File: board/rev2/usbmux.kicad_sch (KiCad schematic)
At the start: 5 parts, among them SW5 MS-22D28-G020, U18 TS3USB30ERSWR, U2 TS3USB30ERSWR

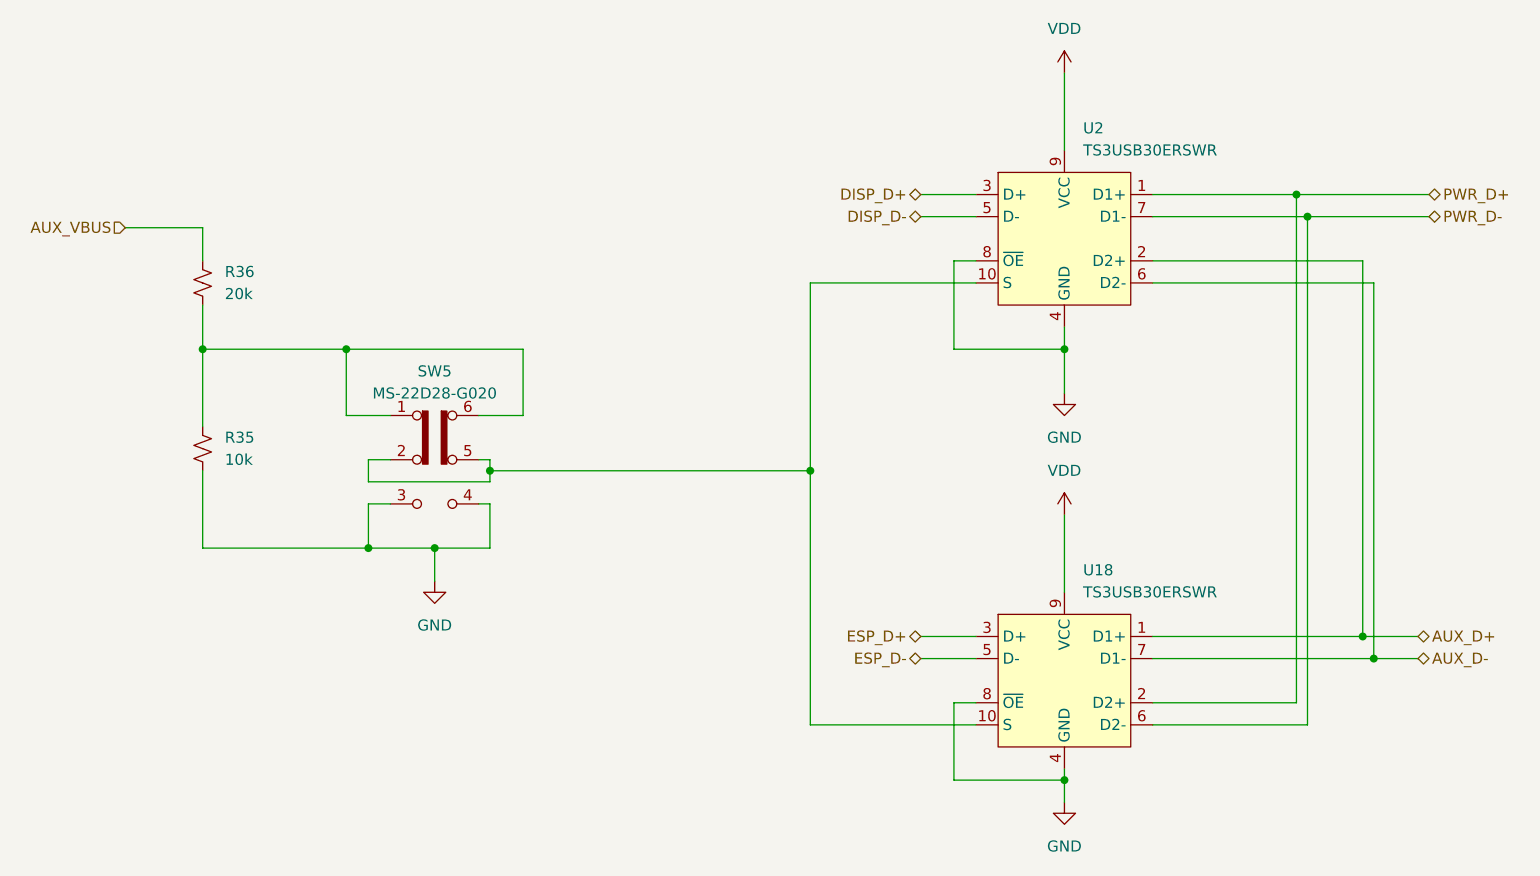
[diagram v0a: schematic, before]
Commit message: Continue board, assign caps/res, adjust for JLC availability
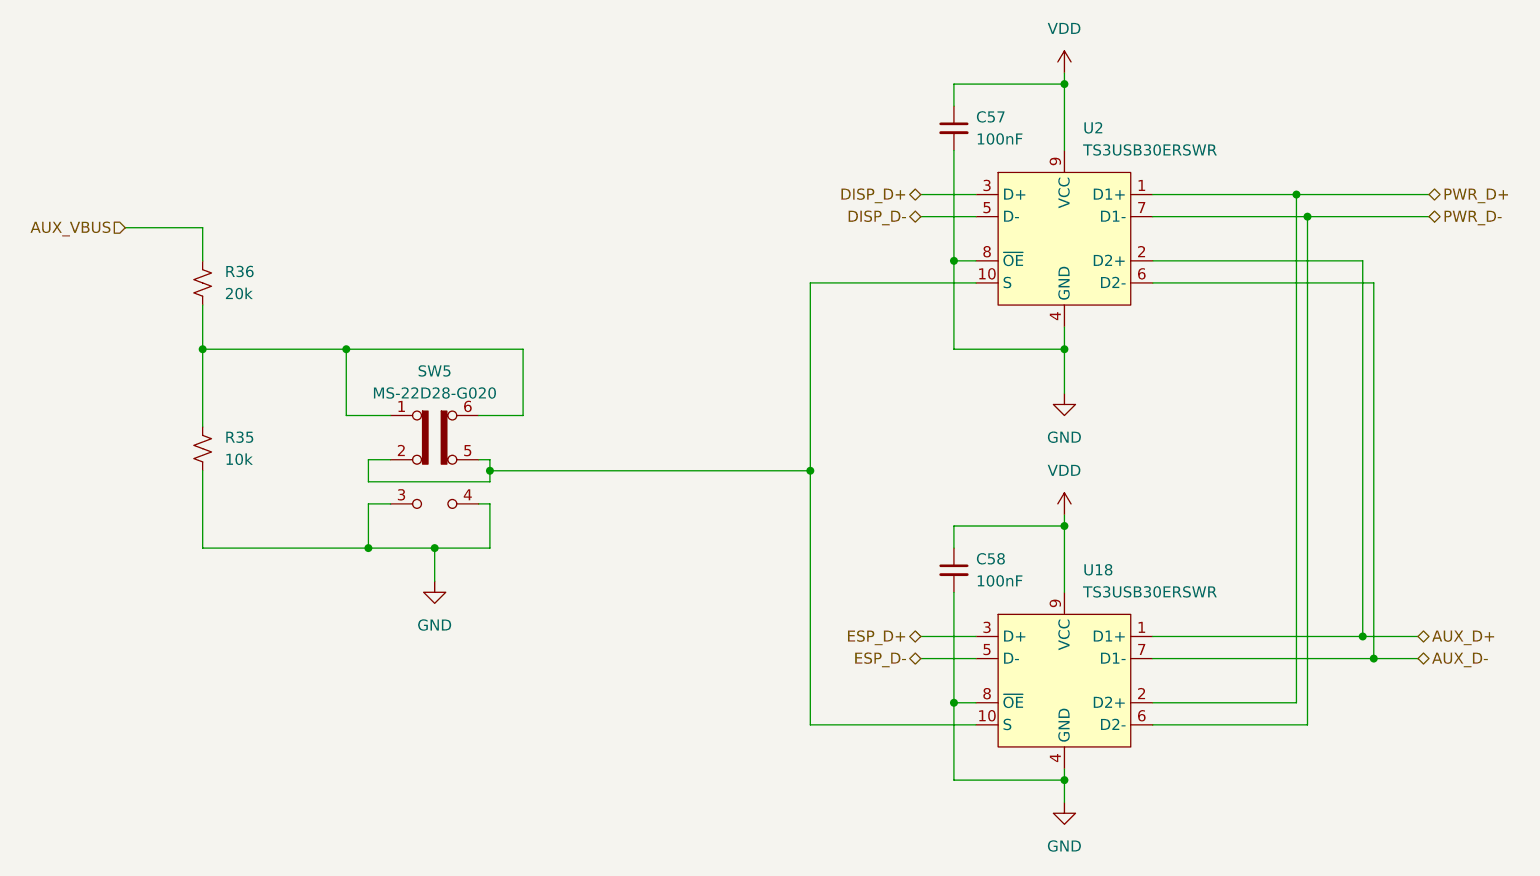
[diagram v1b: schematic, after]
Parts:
- added C57, C58: 100nF, Capacitor_SMD:C_0402_1005Metric, symbol Device:C_Small
- R35: footprint (none) -> Resistor_SMD:R_0805_2012Metric; Part (none) -> 0805W8F1002T5E
- R36: footprint (none) -> Resistor_SMD:R_0603_1608Metric; Part (none) -> 0603WAF2002T5E
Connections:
- net GND: now also C57.2, C58.2
- net VDD: now also C57.1, C58.1

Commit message: Start new PCB
- all footprints setup
- need to setup netclasses next, tho
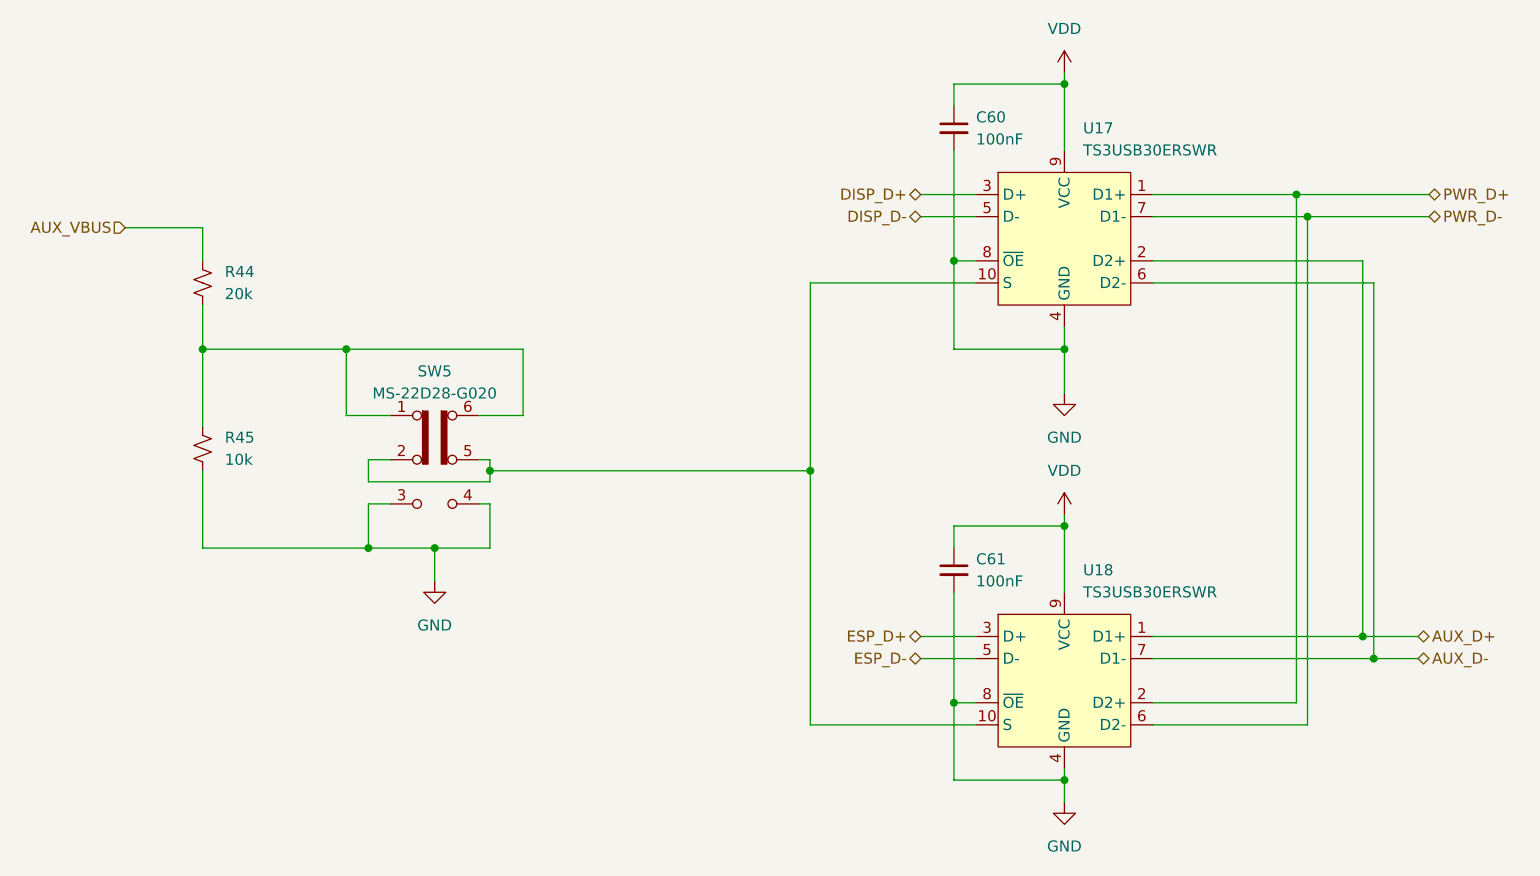
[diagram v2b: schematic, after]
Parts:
- SW5: footprint (none) -> Switch_Slide_SMD:SW-SMD_MS-22D28-G020; Part (none) -> MS-22D28-G020
- U17: renamed from U2; Part (none) -> TS3USB30ERSWR
- U18: Part (none) -> TS3USB30ERSWR
- renumbered C57 to C60, C58 to C61, R36 to R44, R35 to R45
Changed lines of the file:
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@@
 		(dnp no)
 		(fields_autoplaced yes)
-		(property "Reference" "U2"
+		(property "Reference" "U17"
 			(at 172.3233 62.23 0)
 			(effects
@@
 			)
 		)
+		(property "Part" "TS3USB30ERSWR"
+			(at 170.18 74.93 0)
+			(effects
+				(font
+					(size 1.27 1.27)
+				)
+				(hide yes)
+			)
+		)
 		(pin "9"
 		)
@@
 			(project ""
 				(path "/32eb05c7-b4a6-42f3-8fb3-43453631100f/f949a322-cdc0-42f3-8e56-a599c8860839"
-					(reference "U2")
+					(reference "U17")
 					(unit 1)
 				)
@@
 		(dnp no)
 		(fields_autoplaced yes)
-		(property "Reference" "R36"
+		(property "Reference" "R44"
 			(at 73.66 78.7399 0)
 			(effects
@@
 			(project "mainboard"
 				(path "/32eb05c7-b4a6-42f3-8fb3-43453631100f/f949a322-cdc0-42f3-8e56-a599c8860839"
-					(reference "R36")
+					(reference "R44")
 					(unit 1)
 				)
@@
 		(dnp no)
 		(fields_autoplaced yes)
-		(property "Reference" "#PWR031"
+		(property "Reference" "#PWR061"
 			(at 170.18 146.05 0)
 			(effects
@@
 			(project ""
 				(path "/32eb05c7-b4a6-42f3-8fb3-43453631100f/f949a322-cdc0-42f3-8e56-a599c8860839"
-					(reference "#PWR031")
+					(reference "#PWR061")
 					(unit 1)
 				)
@@
 		(dnp no)
 		(fields_autoplaced yes)
-		(property "Reference" "#PWR044"
+		(property "Reference" "#PWR057"
 			(at 97.79 120.65 0)
 			(effects
@@
 			(project ""
 				(path "/32eb05c7-b4a6-42f3-8fb3-43453631100f/f949a322-cdc0-42f3-8e56-a599c8860839"
-					(reference "#PWR044")
+					(reference "#PWR057")
 					(unit 1)
 				)
@@
 		(dnp no)
 		(fields_autoplaced yes)
-		(property "Reference" "C58"
+		(property "Reference" "C61"
 			(at 160.02 111.7662 0)
 			(effects
@@
 			(project "mainboard"
 				(path "/32eb05c7-b4a6-42f3-8fb3-43453631100f/f949a322-cdc0-42f3-8e56-a599c8860839"
-					(reference "C58")
+					(reference "C61")
 					(unit 1)
 				)
@@
 			)
 		)
+		(property "Part" "TS3USB30ERSWR"
+			(at 170.18 125.73 0)
+			(effects
+				(font
+					(size 1.27 1.27)
+				)
+				(hide yes)
+			)
+		)
 		(pin "9"
 		)
@@
 		(dnp no)
 		(fields_autoplaced yes)
-		(property "Reference" "#PWR019"
+		(property "Reference" "#PWR059"
 			(at 170.18 99.06 0)
 			(effects
@@
 			(project ""
 				(path "/32eb05c7-b4a6-42f3-8fb3-43453631100f/f949a322-cdc0-42f3-8e56-a599c8860839"
-					(reference "#PWR019")
+					(reference "#PWR059")
 					(unit 1)
 				)
@@
 		(dnp no)
 		(fields_autoplaced yes)
-		(property "Reference" "C57"
+		(property "Reference" "C60"
 			(at 160.02 60.9662 0)
 			(effects
@@
 			(project ""
 				(path "/32eb05c7-b4a6-42f3-8fb3-43453631100f/f949a322-cdc0-42f3-8e56-a599c8860839"
-					(reference "C57")
+					(reference "C60")
 					(unit 1)
 				)
@@
 		(dnp no)
 		(fields_autoplaced yes)
-		(property "Reference" "R35"
+		(property "Reference" "R45"
 			(at 73.66 97.7899 0)
 			(effects
@@
 			(project ""
 				(path "/32eb05c7-b4a6-42f3-8fb3-43453631100f/f949a322-cdc0-42f3-8e56-a599c8860839"
-					(reference "R35")
+					(reference "R45")
 					(unit 1)
 				)
@@
 		(dnp no)
 		(fields_autoplaced yes)
-		(property "Reference" "#PWR043"
+		(property "Reference" "#PWR060"
 			(at 170.18 110.49 0)
 			(effects
@@
 			(project "mainboard"
 				(path "/32eb05c7-b4a6-42f3-8fb3-43453631100f/f949a322-cdc0-42f3-8e56-a599c8860839"
-					(reference "#PWR043")
+					(reference "#PWR060")
 					(unit 1)
 				)
@@
 			)
 		)
-		(property "Footprint" ""
+		(property "Footprint" "Switch_Slide_SMD:SW-SMD_MS-22D28-G020"
 			(at 111.76 95.25 0)
 			(effects
@@
 			)
 		)
+		(property "Part" "MS-22D28-G020"
+			(at 97.79 100.33 0)
+			(effects
+				(font
+					(size 1.27 1.27)
+				)
+				(hide yes)
+			)
+		)
 		(pin "5"
 		)
@@
 		(dnp no)
 		(fields_autoplaced yes)
-		(property "Reference" "#PWR018"
+		(property "Reference" "#PWR058"
 			(at 170.18 59.69 0)
 			(effects
@@
 			(project ""
 				(path "/32eb05c7-b4a6-42f3-8fb3-43453631100f/f949a322-cdc0-42f3-8e56-a599c8860839"
-					(reference "#PWR018")
-					(unit 1)
-				)
+					(reference "#PWR058")
+					(unit 1)
+				)

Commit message: Really finish rev2 board schematic
- fix some more footprints
  - move to real SD card holder, for example
- repair part numbers
- add LCSC part refs to everything
- add even more caps to the 3.3V reg output
  - really should use an LDO but meh it should be fine

total BOM cost for 5 of them is apparently 160 CAD, or like 32 dollars
each (don't think that includes the feeder fees tho)
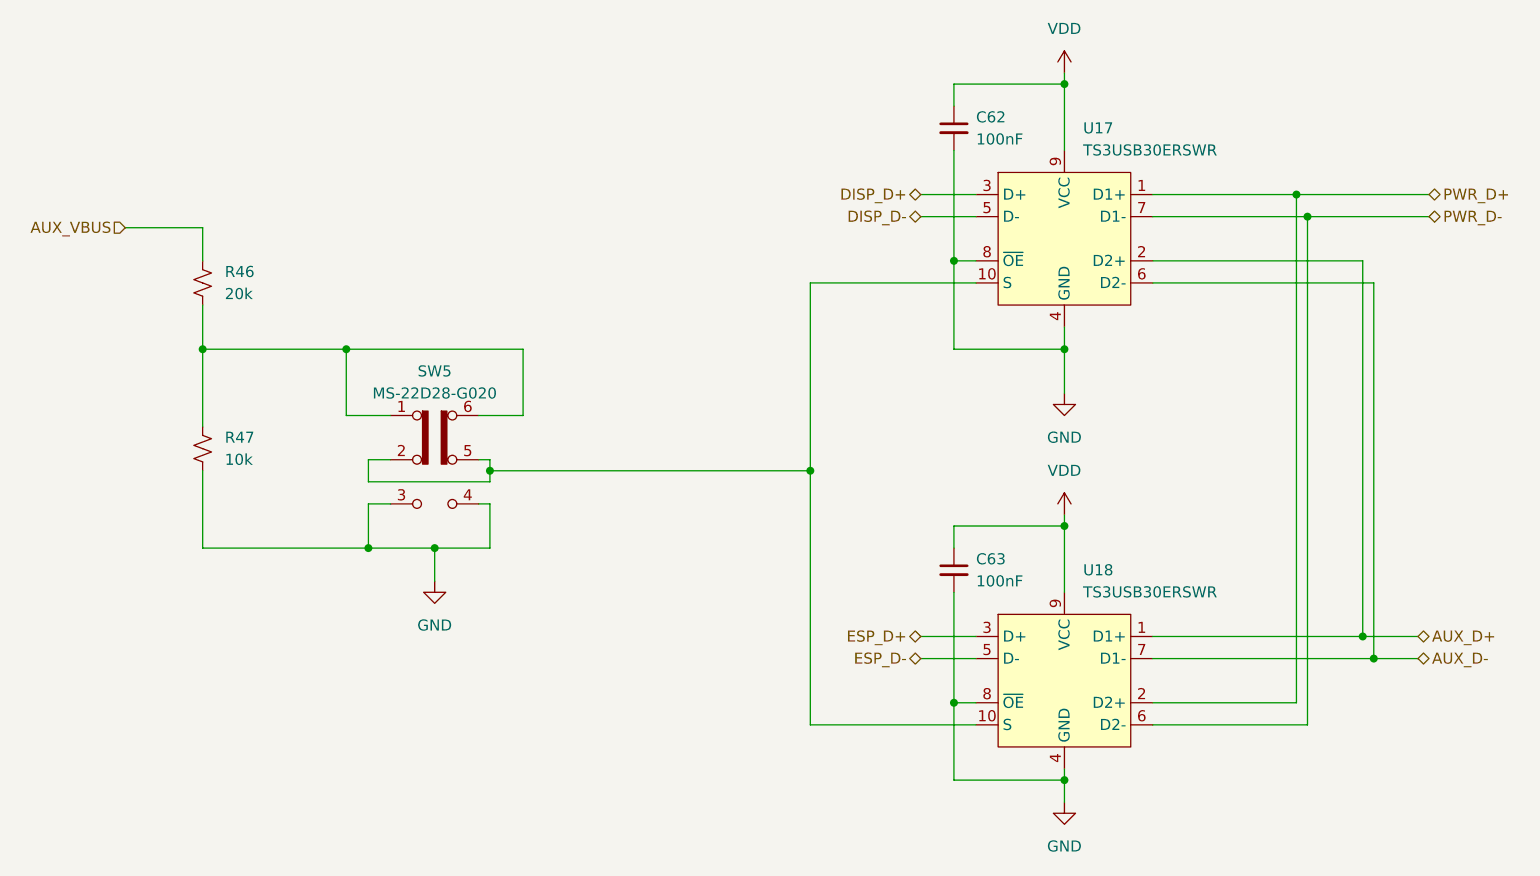
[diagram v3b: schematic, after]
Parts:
- C62: renamed from C60; LCSC (none) -> C307331
- C63: renamed from C61; LCSC (none) -> C307331
- R46: renamed from R44; LCSC (none) -> C4184
- R47: renamed from R45; LCSC (none) -> C17414
- SW5: LCSC (none) -> C963205
- U17, U18: LCSC (none) -> C73880
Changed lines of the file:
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@@
+			)
+		)
+		(property "LCSC" "C73880 "
+			(at 170.18 74.93 0)
+			(effects
+				(font
+					(size 1.27 1.27)
+				)
+				(hide yes)
 			)
 		)
@@
 		(dnp no)
 		(fields_autoplaced yes)
-		(property "Reference" "R44"
+		(property "Reference" "R46"
 			(at 73.66 78.7399 0)
 			(effects
@@
 			)
 		)
+		(property "LCSC" "C4184"
+			(at 71.12 80.01 0)
+			(effects
+				(font
+					(size 1.27 1.27)
+				)
+				(hide yes)
+			)
+		)
 		(pin "1"
 		)
@@
 			(project "mainboard"
 				(path "/32eb05c7-b4a6-42f3-8fb3-43453631100f/f949a322-cdc0-42f3-8e56-a599c8860839"
-					(reference "R44")
+					(reference "R46")
 					(unit 1)
 				)
@@
 		(dnp no)
 		(fields_autoplaced yes)
-		(property "Reference" "#PWR061"
+		(property "Reference" "#PWR062"
 			(at 170.18 146.05 0)
 			(effects
@@
 			(project ""
 				(path "/32eb05c7-b4a6-42f3-8fb3-43453631100f/f949a322-cdc0-42f3-8e56-a599c8860839"
-					(reference "#PWR061")
+					(reference "#PWR062")
 					(unit 1)
 				)
@@
 		(dnp no)
 		(fields_autoplaced yes)
-		(property "Reference" "#PWR057"
+		(property "Reference" "#PWR058"
 			(at 97.79 120.65 0)
 			(effects
@@
 			(project ""
 				(path "/32eb05c7-b4a6-42f3-8fb3-43453631100f/f949a322-cdc0-42f3-8e56-a599c8860839"
-					(reference "#PWR057")
+					(reference "#PWR058")
 					(unit 1)
 				)
@@
 		(dnp no)
 		(fields_autoplaced yes)
-		(property "Reference" "C61"
+		(property "Reference" "C63"
 			(at 160.02 111.7662 0)
 			(effects
@@
 			)
 		)
+		(property "LCSC" "C307331 "
+			(at 157.48 113.03 0)
+			(effects
+				(font
+					(size 1.27 1.27)
+				)
+				(hide yes)
+			)
+		)
 		(pin "1"
 		)
@@
 			(project "mainboard"
 				(path "/32eb05c7-b4a6-42f3-8fb3-43453631100f/f949a322-cdc0-42f3-8e56-a599c8860839"
-					(reference "C61")
+					(reference "C63")
 					(unit 1)
 				)
@@
 			)
 		)
+		(property "LCSC" "C73880 "
+			(at 170.18 125.73 0)
+			(effects
+				(font
+					(size 1.27 1.27)
+				)
+				(hide yes)
+			)
+		)
 		(pin "9"
 		)
@@
 		(dnp no)
 		(fields_autoplaced yes)
-		(property "Reference" "#PWR059"
+		(property "Reference" "#PWR060"
 			(at 170.18 99.06 0)
 			(effects
@@
 			(project ""
 				(path "/32eb05c7-b4a6-42f3-8fb3-43453631100f/f949a322-cdc0-42f3-8e56-a599c8860839"
-					(reference "#PWR059")
+					(reference "#PWR060")
 					(unit 1)
 				)
@@
 		(dnp no)
 		(fields_autoplaced yes)
-		(property "Reference" "C60"
+		(property "Reference" "C62"
 			(at 160.02 60.9662 0)
 			(effects
@@
 			)
 		)
+		(property "LCSC" "C307331 "
+			(at 157.48 62.23 0)
+			(effects
+				(font
+					(size 1.27 1.27)
+				)
+				(hide yes)
+			)
+		)
 		(pin "1"
 		)
@@
 			(project ""
 				(path "/32eb05c7-b4a6-42f3-8fb3-43453631100f/f949a322-cdc0-42f3-8e56-a599c8860839"
-					(reference "C60")
+					(reference "C62")
 					(unit 1)
 				)
@@
 		(dnp no)
 		(fields_autoplaced yes)
-		(property "Reference" "R45"
+		(property "Reference" "R47"
 			(at 73.66 97.7899 0)
 			(effects
@@
 			)
 		)
+		(property "LCSC" "C17414 "
+			(at 71.12 99.06 0)
+			(effects
+				(font
+					(size 1.27 1.27)
+				)
+				(hide yes)
+			)
+		)
 		(pin "1"
 		)
@@
 			(project ""
 				(path "/32eb05c7-b4a6-42f3-8fb3-43453631100f/f949a322-cdc0-42f3-8e56-a599c8860839"
-					(reference "R45")
+					(reference "R47")
 					(unit 1)
 				)
@@
 		(dnp no)
 		(fields_autoplaced yes)
-		(property "Reference" "#PWR060"
+		(property "Reference" "#PWR061"
 			(at 170.18 110.49 0)
 			(effects
@@
 			(project "mainboard"
 				(path "/32eb05c7-b4a6-42f3-8fb3-43453631100f/f949a322-cdc0-42f3-8e56-a599c8860839"
-					(reference "#PWR060")
+					(reference "#PWR061")
 					(unit 1)
 				)
@@
 			)
 		)
+		(property "LCSC" "C963205"
+			(at 97.79 100.33 0)
+			(effects
+				(font
+					(size 1.27 1.27)
+				)
+				(hide yes)
+			)
+		)
 		(pin "5"
 		)
@@
 		(dnp no)
 		(fields_autoplaced yes)
-		(property "Reference" "#PWR058"
+		(property "Reference" "#PWR059"
 			(at 170.18 59.69 0)
 			(effects
@@
 			(project ""
 				(path "/32eb05c7-b4a6-42f3-8fb3-43453631100f/f949a322-cdc0-42f3-8e56-a599c8860839"
-					(reference "#PWR058")
-					(unit 1)
-				)
+					(reference "#PWR059")
+					(unit 1)
+				)
